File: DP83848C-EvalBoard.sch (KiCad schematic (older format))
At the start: 11 parts

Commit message: Component placement
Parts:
- removed J? (x2): Conn_02x08_Counter_Clockwise, symbol Connector_Generic:Conn_02x08_Counter_Clockwise
- removed J? (x4): Conn_02x04_Counter_Clockwise, symbol Connector_Generic:Conn_02x04_Counter_Clockwise
- removed J?: Conn_01x02, symbol Connector_Generic:Conn_01x02
- added J1, J2: Conn_02x08_Odd_Even, Connector_PinHeader_2.54mm:PinHeader_2x08_P2.54mm_Vertical, symbol Connector_Generic:Conn_02x08_Odd_Even
- added J3, J6, J7, J8: Conn_02x04_Odd_Even, Connector_PinHeader_2.54mm:PinHeader_2x04_P2.54mm_Vertical, symbol Connector_Generic:Conn_02x04_Odd_Even
- added R64, R65, R66, R67, R68, R69, R70, R71, R72, R73, R74, R75, R76, R77, R78, R79, R80, R81, R82, R83, R84, R85, R86, R87, R88, R89, R90, R91, R92, R93, R94, R95, R96, R97: 33, Resistor_SMD:R_1206_3216Metric, symbol Device:R_Small
- J4, J5: renamed from J?; footprint (none) -> Connector_PinHeader_2.54mm:PinHeader_1x04_P2.54mm_Vertical
- R1, R2: renamed from R?; footprint (none) -> Resistor_SMD:R_0402_1005Metric
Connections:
- wire segments 120 -> 146
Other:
- moved on the sheet: J4, J5, R1, R2

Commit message: Placement
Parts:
- added J13: Conn_01x04, Connector_PinHeader_2.54mm:PinHeader_1x04_P2.54mm_Vertical, symbol Connector_Generic:Conn_01x04
- added J14: Conn_02x04_Odd_Even, Connector_PinHeader_2.54mm:PinHeader_2x04_P2.54mm_Vertical, symbol Connector_Generic:Conn_02x04_Odd_Even
- added R100, R101, R102, R103, R30, R31: 33, Resistor_SMD:R_0805_2012Metric, symbol Device:R_Small
- R64, R65, R66, R67, R68, R69, R70, R71, R72, R73, R74, R75, R76, R77, R78, R79, R80, R81, R82, R83, R84, R85, R86, R87, R88, R89, R90, R91, R92, R93, R94, R95, R96, R97: footprint Resistor_SMD:R_1206_3216Metric -> Resistor_SMD:R_0805_2012Metric
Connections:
- net +3V3: now also J13.1 (Pin_1), J14.2 (Pin_2), J14.4 (Pin_4)
- net GND: now also J13.4 (Pin_4), J14.6 (Pin_6), J14.8 (Pin_8)
- net MCU/SPI3_MISO: now also R100.2
- net MCU/SPI3_MOSI: now also R101.2
- net MCU/SPI3_NSS: now also R103.2
- net MCU/SPI3_SCK: now also R102.2
- net MCU/USART3_RX: now also R30.1
- net MCU/USART3_TX: now also R31.1
- new net: J14.1 (Pin_1), R100.1
- new net: J14.3 (Pin_3), R101.1
- new net: J14.5 (Pin_5), R102.1
- new net: J14.7 (Pin_7), R103.1
- new net: J13.2 (Pin_2), R30.2
- new net: J13.3 (Pin_3), R31.2

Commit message: Routing
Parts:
- added H1, H2, H3, H4: MountingHole_Pad, MountingHole:MountingHole_3.2mm_M3_Pad_Via, symbol Mechanical:MountingHole_Pad
- R1, R2: footprint Resistor_SMD:R_0402_1005Metric -> Resistor_SMD:R_0603_1608Metric
- R100, R101, R102, R103, R30, R31, R64, R65, R66, R67, R68, R69, R70, R71, R72, R73, R74, R75, R76, R77, R78, R79, R80, R81, R82, R83, R84, R85, R86, R87, R88, R89, R90, R91, R92, R93, R94, R95, R96, R97: footprint Resistor_SMD:R_0805_2012Metric -> Resistor_SMD:R_0603_1608Metric
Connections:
- net +3V3: now also R1.1, R2.1; no longer J8.2 (Pin_2), J8.8 (Pin_8)
- net MCU/I2C1_SCL: now also R96.2; no longer R97.2
- net MCU/I2C1_SDA: now also R97.2; no longer R96.2
- net MCU/USART3_RX: now also R31.1; no longer R30.1
- net MCU/USART3_TX: now also R30.1; no longer R31.1
- net GPIO0_R: now reaches J1.1 (Pin_1), R64.2
- net GPIO5_R: now reaches J1.11 (Pin_11), R69.2
- net GPIO6_R: now reaches J1.13 (Pin_13), R70.2
- net GPIO7_R: now reaches J1.15 (Pin_15), R71.2
- net GPIO1_R: now reaches J1.3 (Pin_3), R65.2
- net GPIO2_R: now reaches J1.5 (Pin_5), R66.2
- net GPIO3_R: now reaches J1.7 (Pin_7), R67.2
- net GPIO4_R: now reaches J1.9 (Pin_9), R68.2
- net ADC0_R: now reaches J2.1 (Pin_1), R72.2
- net ADC5_R: now reaches J2.11 (Pin_11), R77.2
- net ADC6_R: now reaches J2.13 (Pin_13), R78.2
- net ADC7_R: now reaches J2.15 (Pin_15), R79.2
- net ADC1_R: now reaches J2.3 (Pin_3), R73.2
- net ADC2_R: now reaches J2.5 (Pin_5), R74.2
- net ADC3_R: now reaches J2.7 (Pin_7), R75.2
- net ADC4_R: now reaches J2.9 (Pin_9), R76.2
- net TMR1_R: now reaches J3.1 (Pin_1), R80.2
- net TMR2_R: now reaches J3.3 (Pin_3), R81.2
- net TMR3_R: now reaches J3.5 (Pin_5), R82.2
- net TMR4_R: now reaches J3.7 (Pin_7), R83.2
- net SPI1_MISO_R: now reaches J6.1 (Pin_1), R88.1
- net SPI1_MOSI_R: now reaches J6.3 (Pin_3), R89.1
- net SPI1_SCK_R: now reaches J6.5 (Pin_5), R90.1
- net SPI1_NSS: now reaches J6.7 (Pin_7), R91.1
- net SPI2_MISO_R: now reaches J7.1 (Pin_1), R92.1
- net SPI2_MOSI_R: now reaches J7.3 (Pin_3), R93.1
- net SPI2_SCK_R: now reaches J7.5 (Pin_5), R94.1
- net SPI2_NSS_R: now reaches J7.7 (Pin_7), R95.1
- net I2C1_SCL_R: now reaches J8.3 (Pin_3), R96.1
- net I2C1_SCL_R: now also J8.4 (Pin_4); no longer R2.2
- net I2C1_SDA_R: now reaches J8.5 (Pin_5), R97.1
- net I2C1_SDA_R: now also J8.6 (Pin_6); no longer R1.2
- net USART1_TX_R: now reaches J4.2 (Pin_2), R84.2
- net USART1_RX_R: now reaches J4.3 (Pin_3), R85.2
- net USART2_TX_R: now reaches J5.2 (Pin_2), R86.2
- net USART2_RX_R: now reaches J5.3 (Pin_3), R87.2
- net SPI3_MISO_R: now reaches J14.1 (Pin_1), R100.1
- net SPI3_MOSI_R: now reaches J14.3 (Pin_3), R101.1
- net SPI3_SCK_R: now reaches J14.5 (Pin_5), R102.1
- net SPI3_NSS_R: now reaches J14.7 (Pin_7), R103.1
- net USART3_TX_R: now reaches J13.2 (Pin_2), R30.2
- net USART3_RX_R: now reaches J13.3 (Pin_3), R31.2
- net ADC0 renamed MCU/ADC_IN0
- net ADC1 renamed MCU/ADC_IN3
- net ADC2 renamed MCU/ADC_IN6
- net ADC3 renamed MCU/ADC_IN8
- net ADC4 renamed MCU/ADC_IN9
- net ADC5 renamed MCU/ADC_IN10
- net ADC6 renamed MCU/ADC_IN12
- net ADC7 renamed MCU/ADC_IN13
- net GPIO0 renamed MCU/GPIO0
- net GPIO1 renamed MCU/GPIO1
- net GPIO2 renamed MCU/GPIO2
- net GPIO3 renamed MCU/GPIO3
- net GPIO4 renamed MCU/GPIO4
- net GPIO5 renamed MCU/GPIO5
- net GPIO6 renamed MCU/GPIO6
- net GPIO7 renamed MCU/GPIO7
- net TMR1 renamed MCU/TMR_CH1
- net TMR2 renamed MCU/TMR_CH2
- net TMR3 renamed MCU/TMR_CH3
- net TMR4 renamed MCU/TMR_CH4
- net USART1_RX renamed MCU/USART1_TX
- net USART1_TX renamed MCU/USART1_RX
- net USART2_RX renamed MCU/USART2_TX
- net USART2_TX renamed MCU/USART2_RX
- new net: J8.2 (Pin_2), R1.2
- new net: J8.8 (Pin_8), R2.2
- new net GNDPWR: H1.1, H2.1, H3.1, H4.1
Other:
- moved on the sheet: J1, J13, J14, J2, J3, J4, J5, J6, J7, J8, R1, R100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

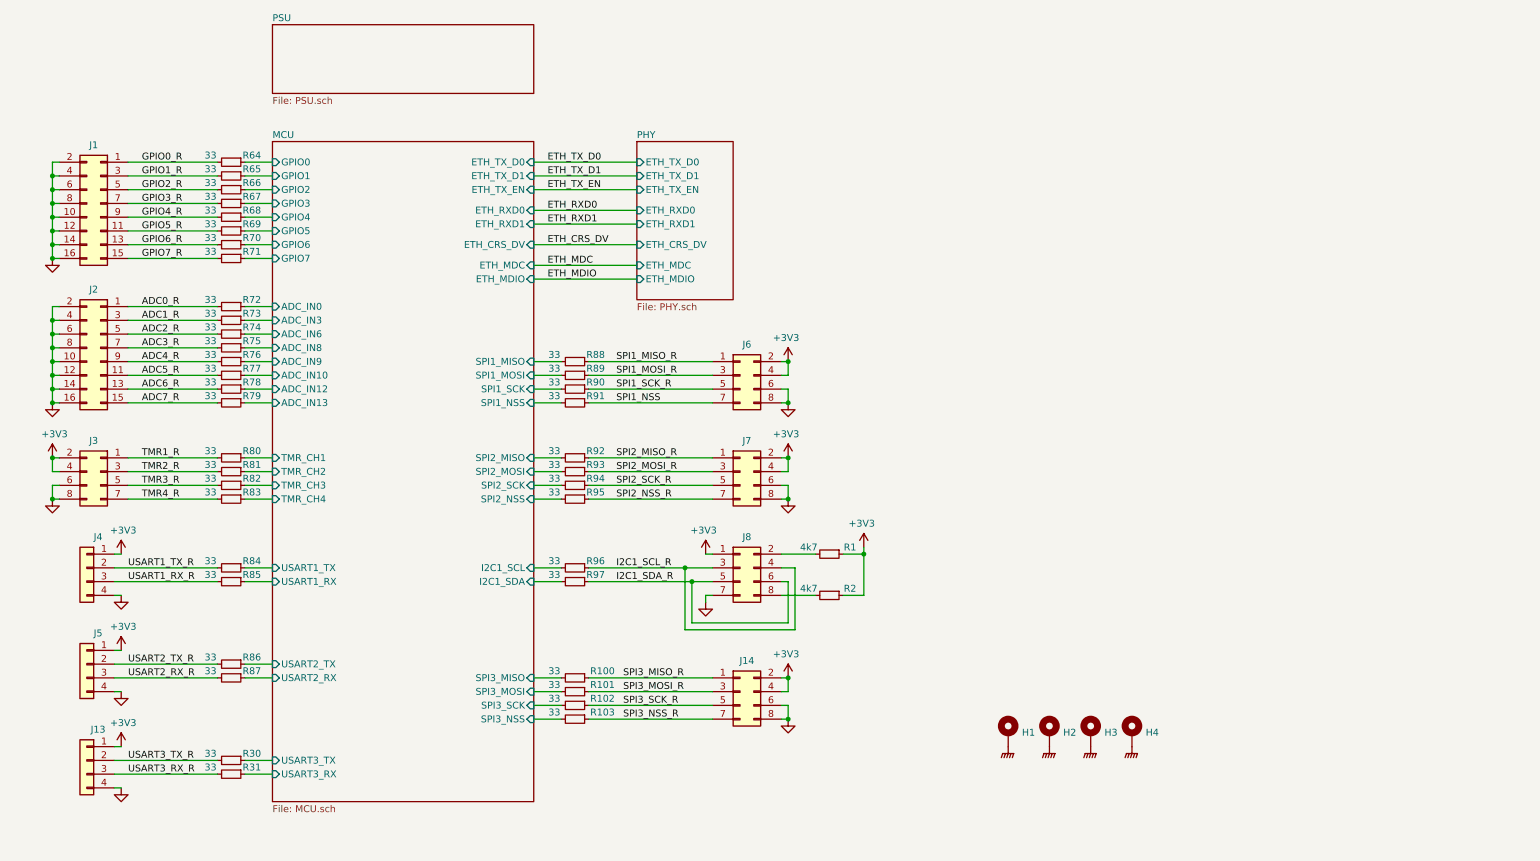
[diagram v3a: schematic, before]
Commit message: Added ESD protection
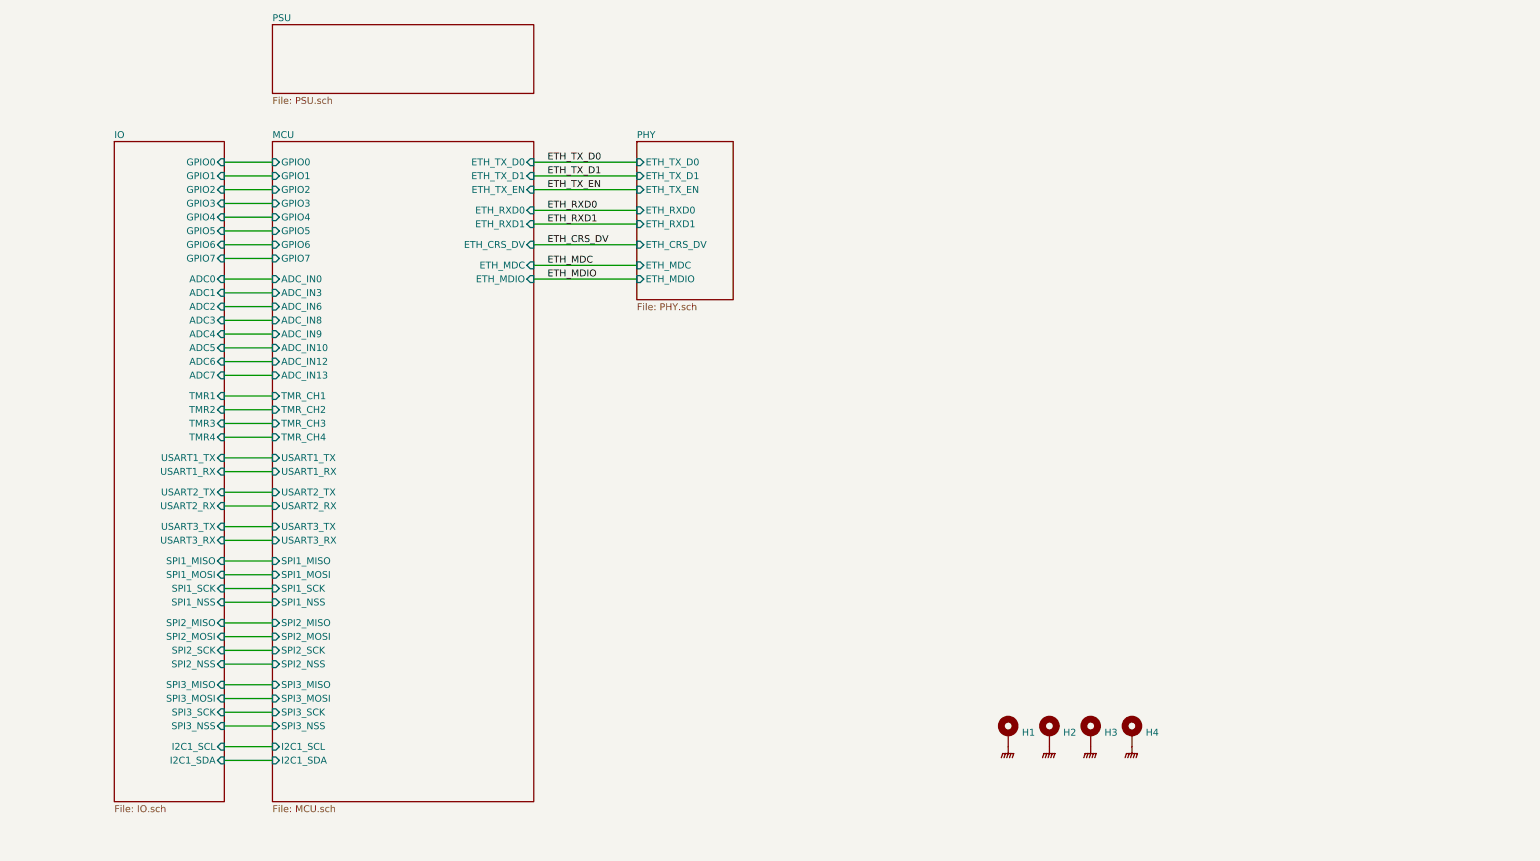
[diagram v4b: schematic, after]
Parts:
- removed J1, J2: Conn_02x08_Odd_Even, Connector_PinHeader_2.54mm:PinHeader_2x08_P2.54mm_Vertical, symbol Connector_Generic:Conn_02x08_Odd_Even
- removed J13, J4, J5: Conn_01x04, Connector_PinHeader_2.54mm:PinHeader_1x04_P2.54mm_Vertical, symbol Connector_Generic:Conn_01x04
- removed J14, J3, J6, J7, J8: Conn_02x04_Odd_Even, Connector_PinHeader_2.54mm:PinHeader_2x04_P2.54mm_Vertical, symbol Connector_Generic:Conn_02x04_Odd_Even
- removed R1, R2: 4k7, Resistor_SMD:R_0603_1608Metric, symbol Device:R_Small
- removed R100, R101, R102, R103, R30, R31, R64, R65, R66, R67, R68, R69, R70, R71, R72, R73, R74, R75, R76, R77, R78, R79, R80, R81, R82, R83, R84, R85, R86, R87, R88, R89, R90, R91, R92, R93, R94, R95, R96, R97: 33, Resistor_SMD:R_0603_1608Metric, symbol Device:R_Small

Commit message: Layout
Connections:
- net GNDPWR renamed Earth
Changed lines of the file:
@@
-	1    0    0    -1
-$EndComp
-$Comp
-L power:GNDPWR #PWR?
-U 1 1 6035A4BE
-P 8450 6150
-AR Path="/6062FABA/6035A4BE" Ref="#PWR?"  Part="1"
-AR Path="/6035A4BE" Ref="#PWR01"  Part="1"
-F 0 "#PWR01" H 8450 5950 50  0001 C CNN
-F 1 "GNDPWR" H 8454 5996 50  0001 C CNN
-F 2 "" H 8450 6100 50  0001 C CNN
-F 3 "" H 8450 6100 50  0001 C CNN
-	1    8450 6150
-	1    0    0    -1
-$EndComp
-$Comp
-L power:GNDPWR #PWR?
-U 1 1 60365884
-P 8750 6150
-AR Path="/6062FABA/60365884" Ref="#PWR?"  Part="1"
-AR Path="/60365884" Ref="#PWR02"  Part="1"
-F 0 "#PWR02" H 8750 5950 50  0001 C CNN
-F 1 "GNDPWR" H 8754 5996 50  0001 C CNN
-F 2 "" H 8750 6100 50  0001 C CNN
-F 3 "" H 8750 6100 50  0001 C CNN
-	1    8750 6150
-	1    0    0    -1
-$EndComp
-$Comp
-L power:GNDPWR #PWR?
-U 1 1 60370B7D
-P 9050 6150
-AR Path="/6062FABA/60370B7D" Ref="#PWR?"  Part="1"
-AR Path="/60370B7D" Ref="#PWR03"  Part="1"
-F 0 "#PWR03" H 9050 5950 50  0001 C CNN
-F 1 "GNDPWR" H 9054 5996 50  0001 C CNN
-F 2 "" H 9050 6100 50  0001 C CNN
-F 3 "" H 9050 6100 50  0001 C CNN
-	1    9050 6150
-	1    0    0    -1
-$EndComp
-$Comp
-L power:GNDPWR #PWR?
-U 1 1 6037BF64
-P 9350 6150
-AR Path="/6062FABA/6037BF64" Ref="#PWR?"  Part="1"
-AR Path="/6037BF64" Ref="#PWR04"  Part="1"
-F 0 "#PWR04" H 9350 5950 50  0001 C CNN
-F 1 "GNDPWR" H 9354 5996 50  0001 C CNN
-F 2 "" H 9350 6100 50  0001 C CNN
-F 3 "" H 9350 6100 50  0001 C CNN
-	1    9350 6150
 	1    0    0    -1
 $EndComp
@@
 Wire Wire Line
 	2750 1900 3100 1900
+$Comp
+L power:Earth #PWR0113
+U 1 1 5FFCE62F
+P 8450 6150
+F 0 "#PWR0113" H 8450 5900 50  0001 C CNN
+F 1 "Earth" H 8450 6000 50  0001 C CNN
+F 2 "" H 8450 6150 50  0001 C CNN
+F 3 "~" H 8450 6150 50  0001 C CNN
+	1    8450 6150
+	1    0    0    -1
+$EndComp
+$Comp
+L power:Earth #PWR0114
+U 1 1 5FFCEB91
+P 8750 6150
+F 0 "#PWR0114" H 8750 5900 50  0001 C CNN
+F 1 "Earth" H 8750 6000 50  0001 C CNN
+F 2 "" H 8750 6150 50  0001 C CNN
+F 3 "~" H 8750 6150 50  0001 C CNN
+	1    8750 6150
+	1    0    0    -1
+$EndComp
+$Comp
+L power:Earth #PWR0115
+U 1 1 5FFCEE61
+P 9050 6150
+F 0 "#PWR0115" H 9050 5900 50  0001 C CNN
+F 1 "Earth" H 9050 6000 50  0001 C CNN
+F 2 "" H 9050 6150 50  0001 C CNN
+F 3 "~" H 9050 6150 50  0001 C CNN
+	1    9050 6150
+	1    0    0    -1
+$EndComp
+$Comp
+L power:Earth #PWR0116
+U 1 1 5FFCF0DF
+P 9350 6150
+F 0 "#PWR0116" H 9350 5900 50  0001 C CNN
+F 1 "Earth" H 9350 6000 50  0001 C CNN
+F 2 "" H 9350 6150 50  0001 C CNN
+F 3 "~" H 9350 6150 50  0001 C CNN
+	1    9350 6150
+	1    0    0    -1
+$EndComp
 $EndSCHEMATC

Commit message: DRC and minor changes
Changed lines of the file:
@@
+	1    0    0    -1
+$EndComp
+$Comp
+L power:Earth #PWR0119
+U 1 1 6016A82E
+P 9850 6150
+F 0 "#PWR0119" H 9850 5900 50  0001 C CNN
+F 1 "Earth" H 9850 6000 50  0001 C CNN
+F 2 "" H 9850 6150 50  0001 C CNN
+F 3 "~" H 9850 6150 50  0001 C CNN
+	1    9850 6150
+	1    0    0    -1
+$EndComp
+$Comp
+L power:PWR_FLAG #FLG0101
+U 1 1 6016A834
+P 9850 6150
+F 0 "#FLG0101" H 9850 6225 50  0001 C CNN
+F 1 "PWR_FLAG" H 9850 6323 50  0000 C CNN
+F 2 "" H 9850 6150 50  0001 C CNN
+F 3 "~" H 9850 6150 50  0001 C CNN
+	1    9850 6150
 	1    0    0    -1
 $EndComp

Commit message: Firmware
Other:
- note added: "Fix:\n- LED series resistors (R1, R3, R42, R45, R46) should be ~~1k\n- connect ethernet ref clock to MCU pin 24 (PA1)\n- R57 should be 33 ohms"
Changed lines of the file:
@@
 	1    0    0    -1
 $EndComp
+Text Notes 5300 4200 0    118  ~ 0
+Fix:\n- LED series resistors (R1, R3, R42, R45, R46)  should be ~~1k\n- connect ethernet ref clock to MCU pin 24 (PA1)\n- R57 should be 33 ohms
 $EndSCHEMATC
